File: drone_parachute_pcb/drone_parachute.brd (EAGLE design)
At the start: 97.8 x 97.8 mm, 33 parts, among them T1 BC547, U1 GY-521MPU6050, U2 AMS1117-3.3

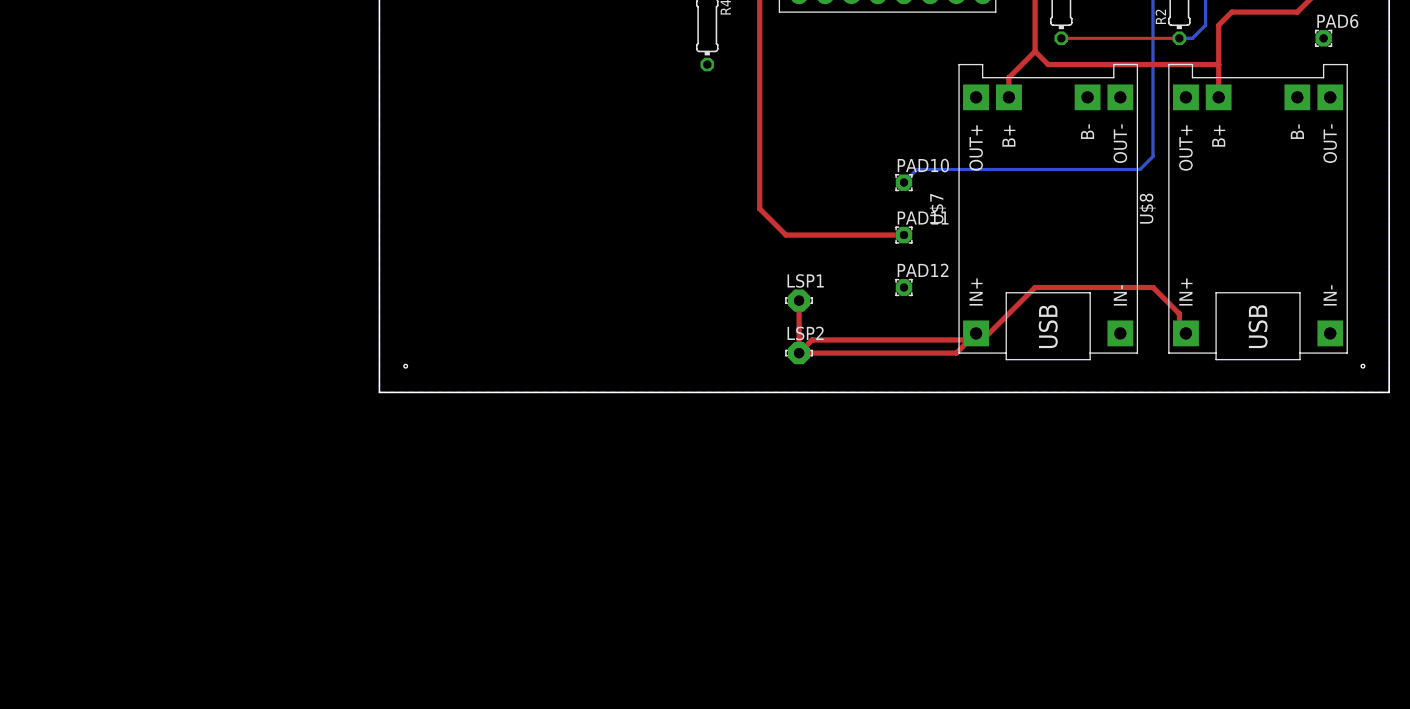
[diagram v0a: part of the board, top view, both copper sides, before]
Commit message: added Ti's charging IC schematic.
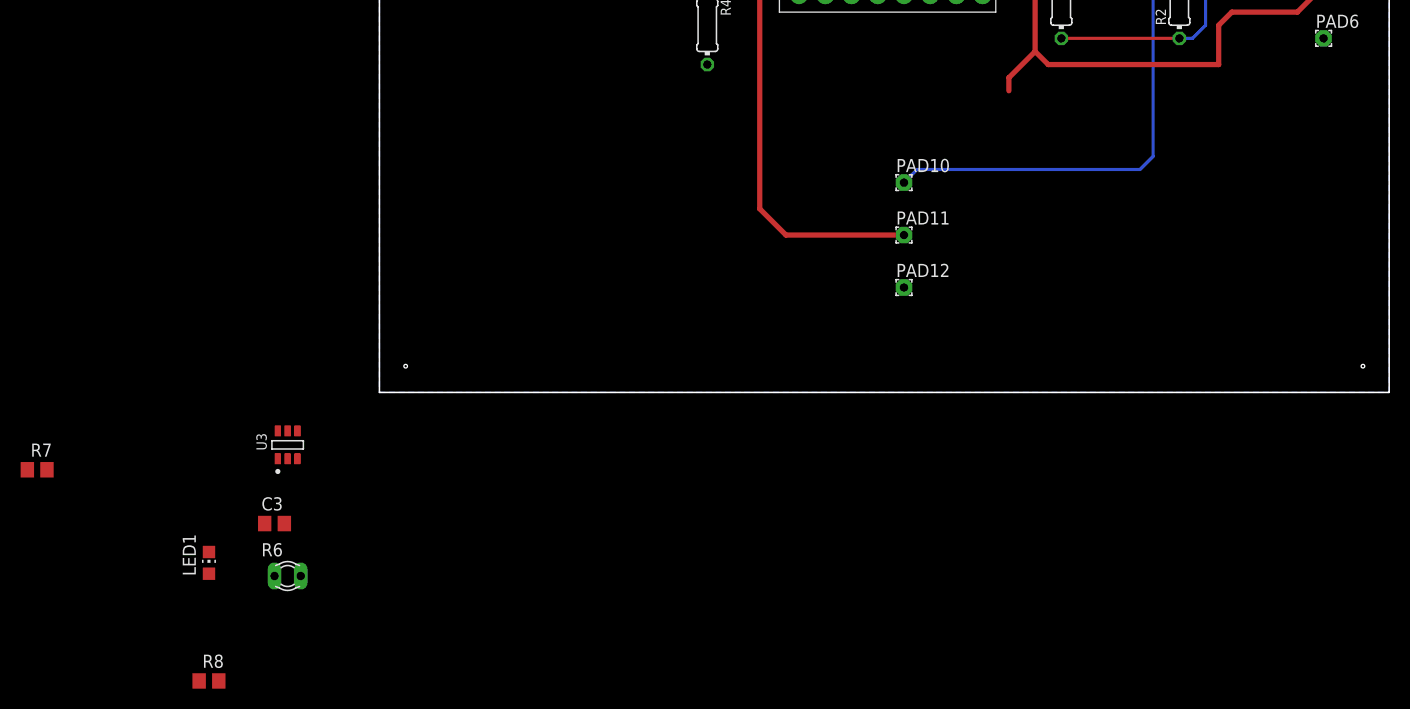
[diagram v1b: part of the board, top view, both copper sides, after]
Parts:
- removed LSP1, LSP2: LSP10, solpad:LSP10
- removed U$7, U$8: BATTERY-CHARGER-LI-PROT, diy-modules:BATTERY-CHARGER-LI-PROT
- added C3: (no value), rcl:C0805
- added LED1: (no value), led:CHIP-LED0805
- added R6: (no value), ptc-ntc:P640
- added R7, R8: (no value), rcl:R0805
- added U3: TEXAS_INSTRUMENTS_BQ21040DBVRTEXAS_INSTRUMENTS_BQ21040DBVR_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, Texas Instruments - BQ21040DBVR:TEXAS_INSTRUMENTS_BQ21040DBVR_0
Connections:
- removed net V+_CHARGING: LSP1.MP, LSP2.MP, U$7.IN+, U$8.IN+
- new net N$11: R7.1, U3.4
- new net N$13: LED1.A, R8.1
- new net N$7: R6.2, U3.1
- new net N$9: LED1.C, U3.3
- net +5V: now also C3.1, U3.6
- net GND: now also C3.2, R6.1, R7.2, U3.5; no longer U$7.B-, U$7.IN-, U$8.B-, U$8.IN-
- net V+_BB: now also R8.2, U3.2; no longer U$7.B+, U$8.B+
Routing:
- net V+_CHARGING: track 65.7 -> 0.00 mm
- net V+_BB: track 89.2 -> 86.0 mm

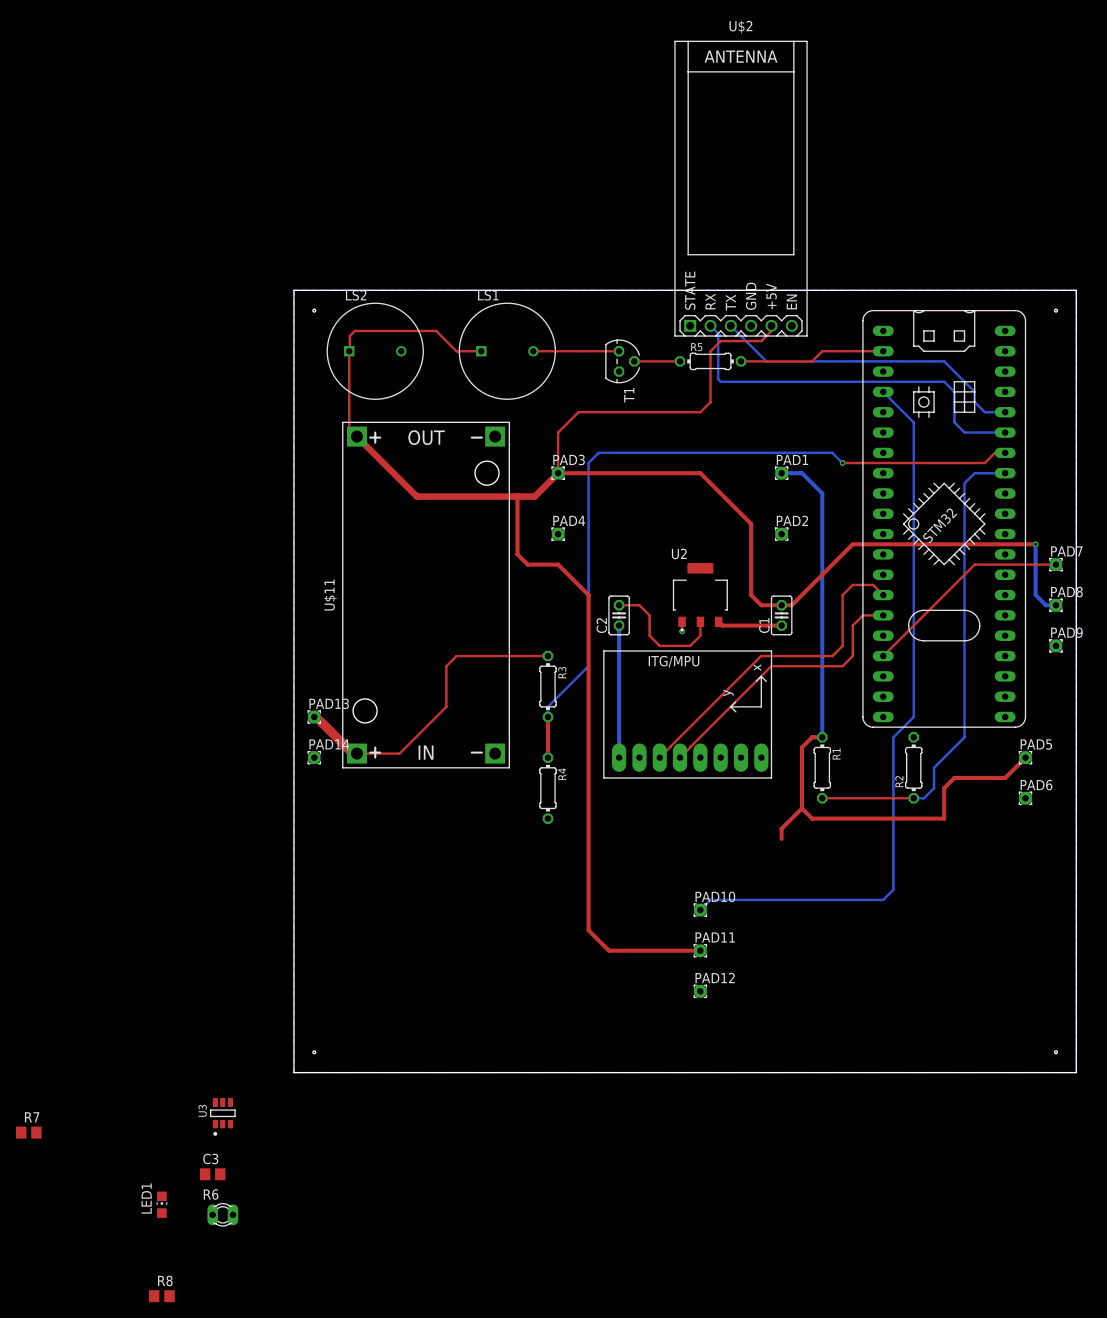
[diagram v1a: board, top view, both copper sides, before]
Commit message: added board .brd for charging IC.
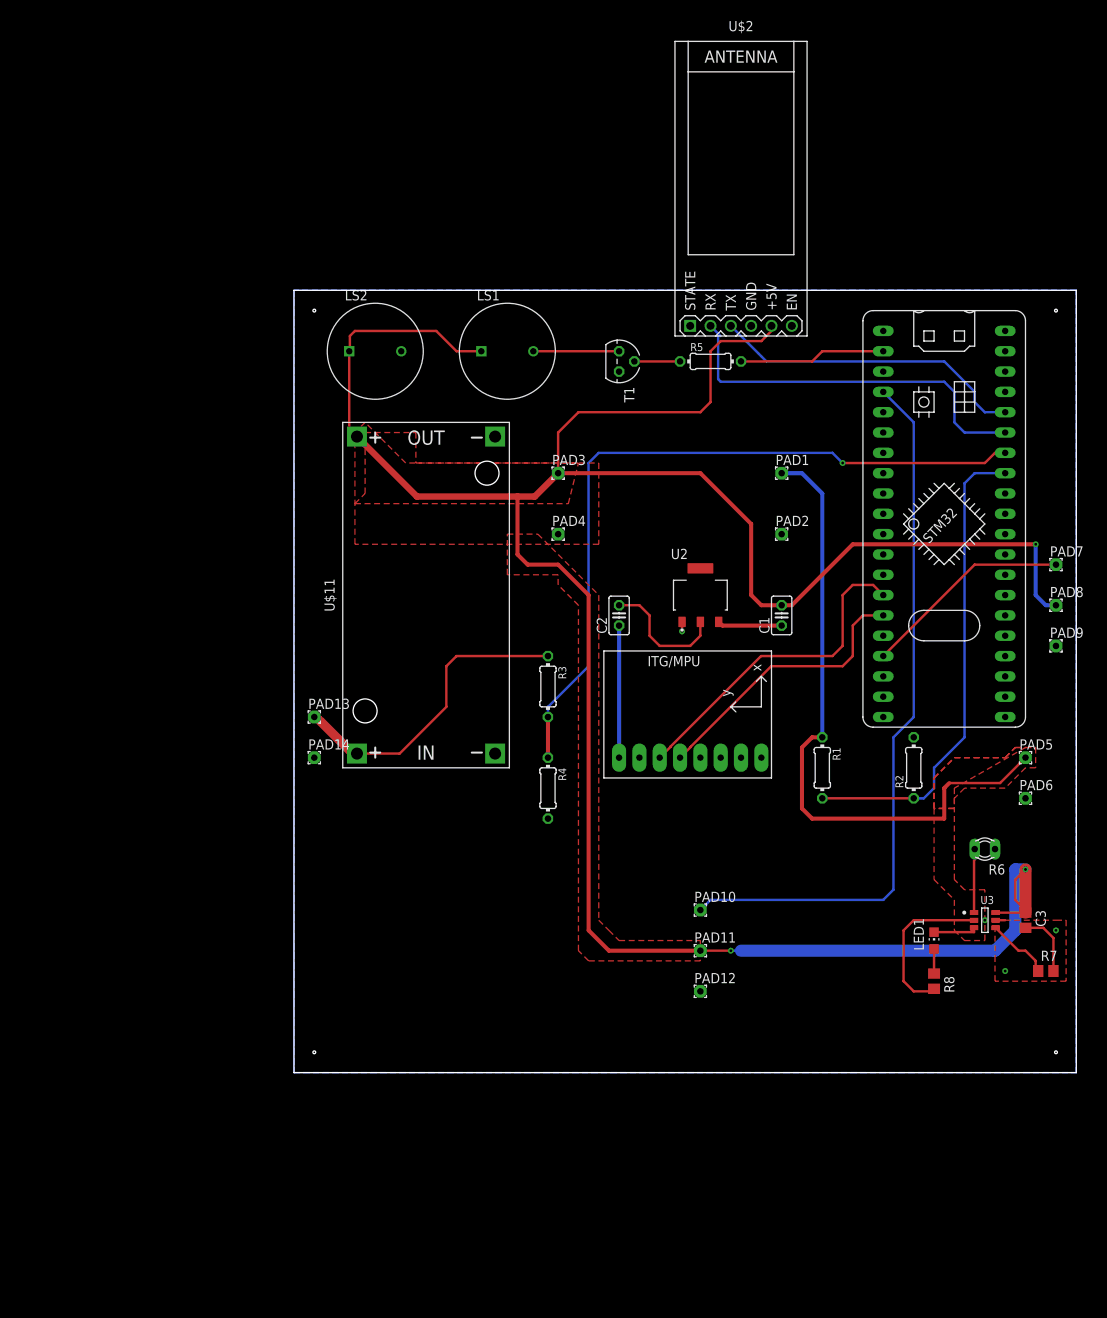
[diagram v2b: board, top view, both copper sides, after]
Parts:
- moved R7 128.7 mm to (94.0, 11.4)
- moved C3 106.4 mm to (91.4, 17.8), turned to 270 degrees
- moved R6 105.7 mm to (86.4, 26.7), turned to 180 degrees
- moved R8 104.2 mm to (80.0, 10.2), turned to 270 degrees
- moved LED1 102.0 mm to (80.0, 15.2)
- moved U3 98.3 mm to (86.4, 17.8), turned to 270 degrees
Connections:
- net N$11 renamed ISET
- net N$7 renamed NTC
- net N$9 renamed CHG_BAR
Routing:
- net GND: track 1.19 -> 401.7 mm
- net +5V: track 261.3 -> 325.9 mm, vias 1 -> 3
- net V+_BB: track 86.0 -> 101.2 mm
- net ISET: track 0.00 -> 8.30 mm
- net NTC: track 0.00 -> 7.97 mm
- net CHG_BAR: track 0.00 -> 5.99 mm
- net N$13: track 0.00 -> 3.08 mm
- added copper zone on layer 1, net +5V
- added copper zone on layer 1, net GND
- added copper zone on layer 1, net V+_BB
